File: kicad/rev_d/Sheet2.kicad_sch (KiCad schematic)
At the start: 226 parts, among them J10 vg_old, J5 external clock, J6 JUMPER, J8 JUMPER, J9 JUMPER, Q2 QUARTZ, Q3 QUARTZ32768, X10 ST-214C, X11 KEYB-MOUSE, X12 IDC20, X13 USB_C, X14 AAFP/AC97 audio, X15 PLB2-2, X16 PLB1-4I, X17 PLB1-4I, X18 PLB1-4I, X19 AVR pgm conn, X20 PLB1-4I, X21 RSA103, X4 IDC10M, X5 IDC10M, X6 RS232_9

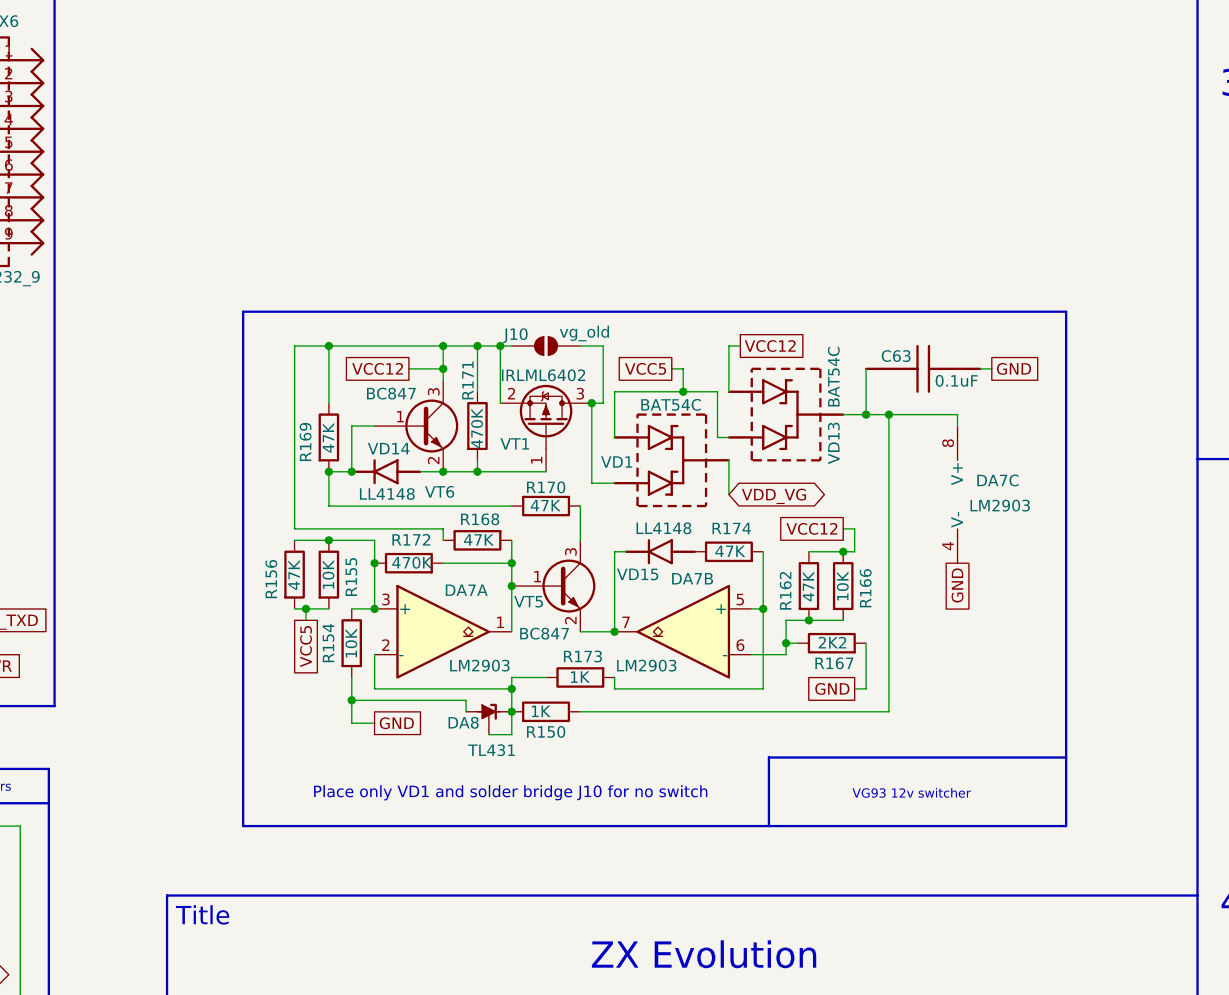
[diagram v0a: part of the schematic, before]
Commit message: pentevo: rev D: for VG 12v switcher, replace paralleled resistors with single ones
git-svn-id: svn://localhost/local-pentevo@1201 c6c76956-fad2-4150-a3a9-ea0a427205ba
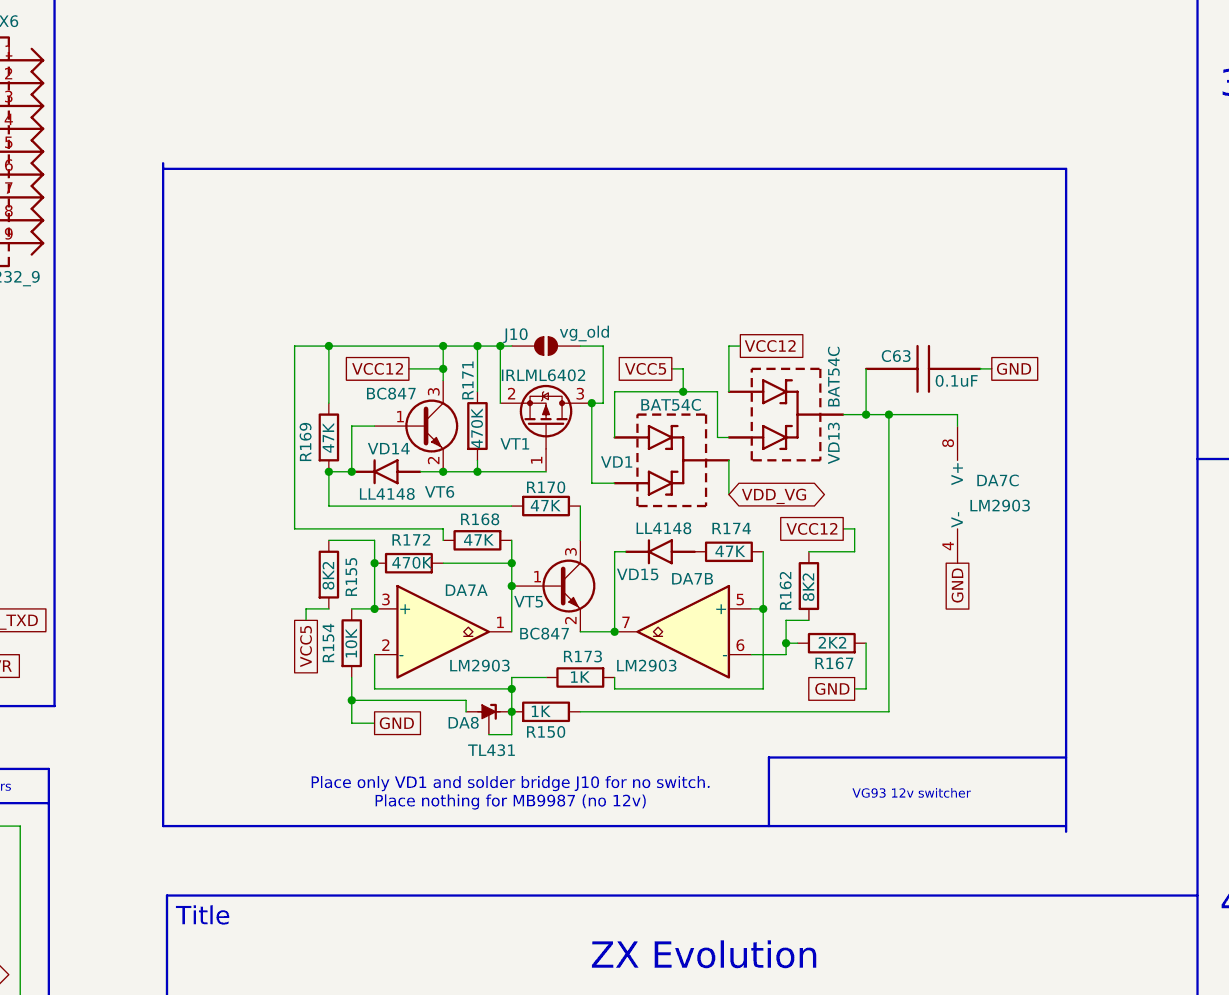
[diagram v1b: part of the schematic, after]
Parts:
- removed R156: 47K, Resistor_SMD:R_0805_2012Metric_Pad1.20x1.40mm_HandSolder, symbol Device:R
- removed R166: 10K, Resistor_SMD:R_0805_2012Metric_Pad1.20x1.40mm_HandSolder, symbol Device:R
- R155: value 10K -> 8K2
- R162: value 47K -> 8K2
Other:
- note added: "Place only VD1 and solder bridge J10 for no switch. Place nothing for MB9987 (no 12v)"
- note removed: "Place only VD1 and solder bridge J10 for no switch"
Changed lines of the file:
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@@
 	)
 	(junction
-		(at 499.11 335.28)
-		(diameter 0)
-		(color 0 0 0 0)
-	)
-	(junction
 		(at 161.29 233.68)
 		(diameter 0)
@@
 	)
 	(junction
-		(at 441.96 334.01)
-		(diameter 0)
-		(color 0 0 0 0)
-	)
-	(junction
 		(at 325.12 306.07)
 		(diameter 0)
@@
 	)
 	(junction
-		(at 439.42 341.63)
-		(diameter 0)
-		(color 0 0 0 0)
-	)
-	(junction
 		(at 492.76 345.44)
 		(diameter 0)
@@
 	)
 	(junction
-		(at 495.3 342.9)
-		(diameter 0)
-		(color 0 0 0 0)
-	)
-	(junction
 		(at 127 266.7)
 		(diameter 0)
@@
 	(wire
 		(pts
-			(xy 495.3 335.28) (xy 499.11 335.28)
+			(xy 495.3 335.28) (xy 500.38 335.28)
 		)
 		(stroke
@@
 	(wire
 		(pts
-			(xy 438.15 341.63) (xy 439.42 341.63)
-		)
-		(stroke
-			(width 0)
-			(type default)
-		)
-	)
-	(wire
-		(pts
 			(xy 383.54 288.29) (xy 384.81 288.29)
 		)
@@
 	(polyline
 		(pts
-			(xy 432.435 365.76) (xy 523.875 365.76)
+			(xy 423.545 365.76) (xy 523.875 365.76)
 		)
 		(stroke
@@
 	(wire
 		(pts
-			(xy 499.11 335.28) (xy 500.38 335.28)
-		)
-		(stroke
-			(width 0)
-			(type default)
-		)
-	)
-	(wire
-		(pts
 			(xy 391.16 213.36) (xy 386.08 213.36)
 		)
@@
 	(polyline
 		(pts
-			(xy 432.435 308.61) (xy 432.435 365.76)
+			(xy 423.545 292.1) (xy 423.545 365.76)
 		)
 		(stroke
@@
 	(wire
 		(pts
-			(xy 438.15 334.01) (xy 441.96 334.01)
-		)
-		(stroke
-			(width 0)
-			(type default)
-		)
-	)
-	(wire
-		(pts
 			(xy 346.71 74.93) (xy 346.71 105.41)
 		)
@@
 	(wire
 		(pts
-			(xy 495.3 342.9) (xy 499.11 342.9)
-		)
-		(stroke
-			(width 0)
-			(type default)
-		)
-	)
-	(wire
-		(pts
 			(xy 154.94 109.22) (xy 154.94 119.38)
 		)
@@
 	(polyline
 		(pts
-			(xy 523.875 365.76) (xy 523.875 308.61)
+			(xy 523.875 366.395) (xy 523.875 292.735)
 		)
 		(stroke
@@
 	(polyline
 		(pts
-			(xy 523.875 308.61) (xy 432.435 308.61)
+			(xy 523.875 292.735) (xy 423.545 292.735)
 		)
 		(stroke
@@
 		)
 	)
-	(text "Place only VD1 and solder bridge J10 for no switch"
+	(text "Place only VD1 and solder bridge J10 for no switch.\nPlace nothing for MB9987 (no 12v)"
 		(exclude_from_sim no)
 		(at 462.153 362.204 0)
@@
 			)
 		)
-		(property "Value" "10K"
+		(property "Value" "8K2"
 			(at 441.96 339.598 90)
 			(effects
@@
 	)
 	(symbol
-		(lib_id "Device:R")
-		(at 499.11 339.09 0)
-		(unit 1)
-		(exclude_from_sim no)
-		(in_bom yes)
-		(on_board yes)
-		(dnp no)
-		(property "Reference" "R166"
-			(at 501.65 341.63 90)
-			(effects
-				(font
-					(size 1.27 1.27)
-				)
-				(justify left)
-			)
-		)
-		(property "Value" "10K"
-			(at 499.11 340.868 90)
-			(effects
-				(font
-					(size 1.27 1.27)
-				)
-				(justify left)
-			)
-		)
-		(property "Footprint" "Resistor_SMD:R_0805_2012Metric_Pad1.20x1.40mm_HandSolder"
-			(at 497.332 339.09 90)
-			(effects
-				(font
-					(size 1.27 1.27)
-				)
-				(hide yes)
-			)
-		)
-		(property "Datasheet" "~"
-			(at 499.11 339.09 0)
-			(effects
-				(font
-					(size 1.27 1.27)
-				)
-				(hide yes)
-			)
-		)
-		(property "Description" "Resistor"
-			(at 499.11 339.09 0)
-			(effects
-				(font
-					(size 1.27 1.27)
-				)
-				(hide yes)
-			)
-		)
-		(pin "2"
-		)
-		(pin "1"
-		)
-		(instances
-			(project "eva"
-				(path "/ab605654-a730-497b-9e09-9b351f74b935/31d5864f-06ec-4c73-9256-780a6880087d"
-					(reference "R166")
-					(unit 1)
-				)
-			)
-		)
-	)
-	(symbol
 		(lib_id "Connector:Conn_01x01_Pin")
 		(at 292.1 213.36 0)
@@
 	)
 	(symbol
-		(lib_id "Device:R")
-		(at 438.15 337.82 0)
-		(unit 1)
-		(exclude_from_sim no)
-		(in_bom yes)
-		(on_board yes)
-		(dnp no)
-		(property "Reference" "R156"
-			(at 435.61 340.614 90)
-			(effects
-				(font
-					(size 1.27 1.27)
-				)
-				(justify left)
-			)
-		)
-		(property "Value" "47K"
-			(at 438.15 339.598 90)
-			(effects
-				(font
-					(size 1.27 1.27)
-				)
-				(justify left)
-			)
-		)
-		(property "Footprint" "Resistor_SMD:R_0805_2012Metric_Pad1.20x1.40mm_HandSolder"
-			(at 436.372 337.82 90)
-			(effects
-				(font
-					(size 1.27 1.27)
-				)
-				(hide yes)
-			)
-		)
-		(property "Datasheet" "~"
-			(at 438.15 337.82 0)
-			(effects
-				(font
-					(size 1.27 1.27)
-				)
-				(hide yes)
-			)
-		)
-		(property "Description" "Resistor"
-			(at 438.15 337.82 0)
-			(effects
-				(font
-					(size 1.27 1.27)
-				)
-				(hide yes)
-			)
-		)
-		(pin "2"
-		)
-		(pin "1"
-		)
-		(instances
-			(project "eva"
-				(path "/ab605654-a730-497b-9e09-9b351f74b935/31d5864f-06ec-4c73-9256-780a6880087d"
-					(reference "R156")
-					(unit 1)
-				)
-			)
-		)
-	)
-	(symbol
 		(lib_id "eva-altium-import:Sheet2_3_RESCHIP")
 		(at 100.33 314.96 0)
@@
 			)
 		)
-		(property "Value" "47K"
+		(property "Value" "8K2"
 			(at 495.3 340.868 90)
 			(effects

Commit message: pentevo: rev D: change VG 12v switcher schematics to have less components
git-svn-id: svn://localhost/local-pentevo@1202 c6c76956-fad2-4150-a3a9-ea0a427205ba
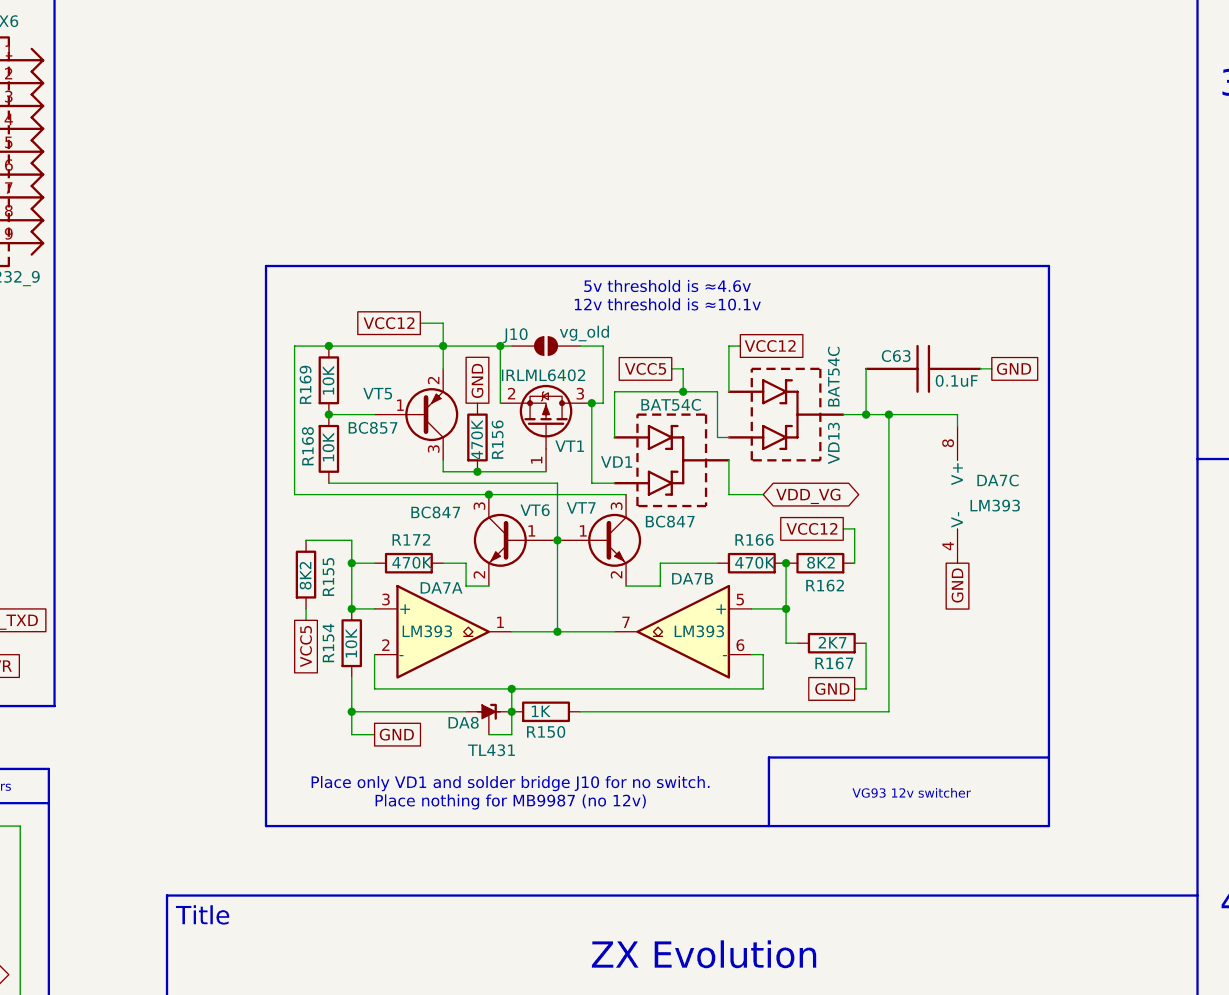
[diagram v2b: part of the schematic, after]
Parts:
- removed R170, R174: 47K, Resistor_SMD:R_0805_2012Metric_Pad1.20x1.40mm_HandSolder, symbol Device:R
- removed R171: 470K, Resistor_SMD:R_0805_2012Metric_Pad1.20x1.40mm_HandSolder, symbol Device:R
- removed R173: 1K, Resistor_SMD:R_0805_2012Metric_Pad1.20x1.40mm_HandSolder, symbol Device:R
- removed VD14, VD15: LL4148, Diode_SMD:D_MiniMELF_Handsoldering, symbol eva-altium-import:Sheet2_0_mirrored_LL4148
- removed VT5: BC847, Package_TO_SOT_SMD:SOT-23_Handsoldering, symbol Transistor_BJT:BC847
- added R156, R166: 470K, Resistor_SMD:R_0805_2012Metric_Pad1.20x1.40mm_HandSolder, symbol Device:R
- added VT5: BC857, Package_TO_SOT_SMD:SOT-23_Handsoldering, symbol Transistor_BJT:BC857
- added VT7: BC847, Package_TO_SOT_SMD:SOT-23, symbol Transistor_BJT:BC847
- DA7: value LM2903 -> LM393
- R167: value 2K2 -> 2K7
- R168, R169: value 47K -> 10K
- VT6: footprint Package_TO_SOT_SMD:SOT-23_Handsoldering -> Package_TO_SOT_SMD:SOT-23
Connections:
- net GND: now also R156.1
- net VCC12: now also R162.2, VT5.2 (E), VT7.3 (C); no longer R162.1, R168.1
- net at DA7.7: now also DA7.1, R168.1, VT6.1 (B), VT7.1 (B)
- net at DA7.5 (+): now also R162.1, R167.1, R166.2
- net at VT6.2 (E): now also R172.2; no longer VT1.1 (G)
- net at R169.2: now also R168.2, VT5.1 (B); no longer VT6.1 (B)
- net at DA7.2 (-), DA8.1 (K), DA8.2 (REF)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: now also DA7.6 (-)
- new net: R166.1, VT7.2 (E)
- new net: R156.2, VT1.1 (G), VT5.3 (C)
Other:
- note added: "5v threshold is ≈4.6v 12v threshold is ≈10.1v"
- moved on the sheet: R155, R162, R169

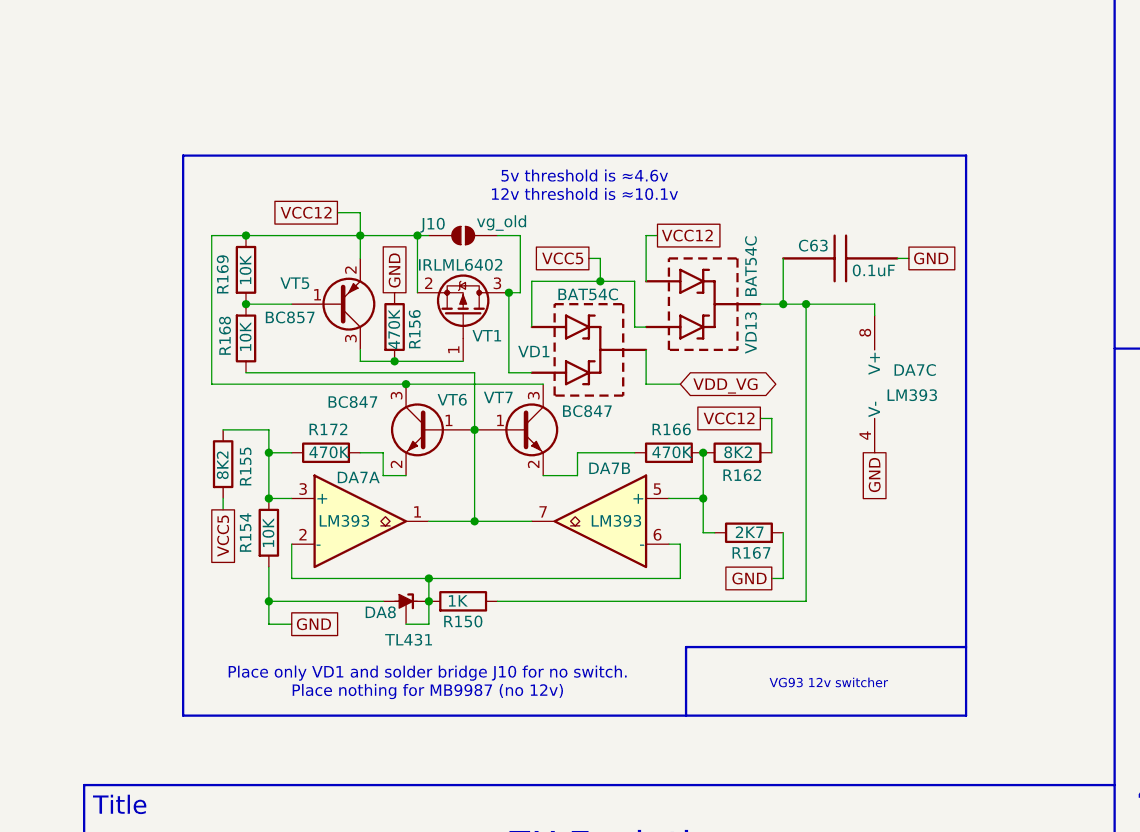
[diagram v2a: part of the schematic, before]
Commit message: pentevo: rev D: change VG 12v switcher schematics to using 2xPST529C, results in significantly less components
git-svn-id: svn://localhost/local-pentevo@1205 c6c76956-fad2-4150-a3a9-ea0a427205ba
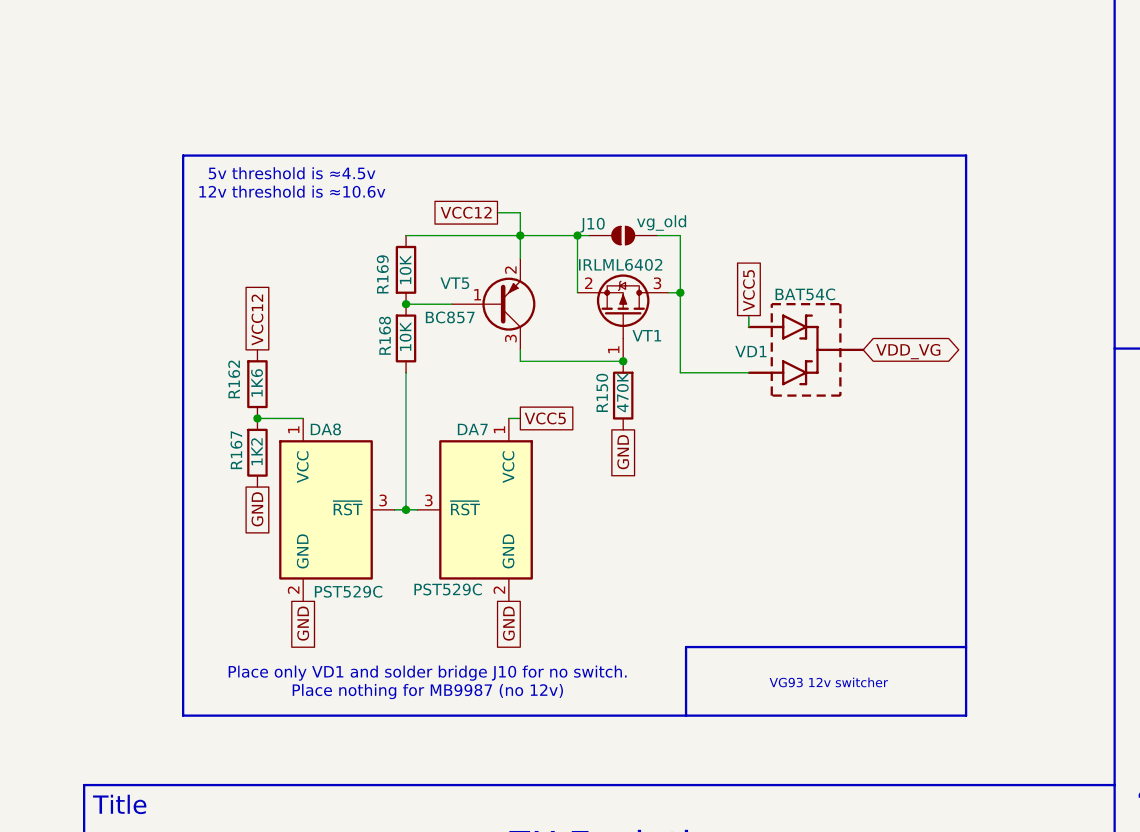
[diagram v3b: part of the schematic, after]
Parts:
- removed C63: 0.1uF, Capacitor_SMD:C_0805_2012Metric_Pad1.18x1.45mm_HandSolder, symbol eva-altium-import:Sheet1_0_CAPCHIP
- removed DA7: LM393, Package_SO:SOIC-8_3.9x4.9mm_P1.27mm, symbol Comparator:LM2903
- removed DA8: TL431, Package_TO_SOT_SMD:SOT-23_Handsoldering, symbol Reference_Voltage:TL431DBZ
- removed R154: 10K, Resistor_SMD:R_0805_2012Metric_Pad1.20x1.40mm_HandSolder, symbol Device:R
- removed R155: 8K2, Resistor_SMD:R_0805_2012Metric_Pad1.20x1.40mm_HandSolder, symbol Device:R
- removed R156, R166, R172: 470K, Resistor_SMD:R_0805_2012Metric_Pad1.20x1.40mm_HandSolder, symbol Device:R
- removed VD13: BAT54C, Package_TO_SOT_SMD:SOT-23_Handsoldering, symbol eva-altium-import:Sheet1_2_BAT54C
- removed VT6, VT7: BC847, Package_TO_SOT_SMD:SOT-23, symbol Transistor_BJT:BC847
- added DA7, DA8: PST529C, Package_TO_SOT_THT:TO-92_HandSolder, symbol eva-altium-import:PST529C
- R150: value 1K -> 470K
- R162: value 8K2 -> 1K6
- R167: value 2K7 -> 1K2
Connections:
- net GND: now also R150.1, R167.1, DA7.2 (GND), DA8.2 (GND); no longer R167.2
- net VCC5: now also DA7.1 (VCC)
- net at R162.1: now also R167.2, DA8.1 (VCC); no longer R167.1
- net at R168.1: now also DA7.3 (~{RST}), DA8.3 (~{RST})
- net at R150.2: now also VT1.1 (G), VT5.3 (C)
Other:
- note added: "5v threshold is ≈4.5v 12v threshold is ≈10.6v"
- note removed: "5v threshold is ≈4.6v 12v threshold is ≈10.1v"
- moved on the sheet: J10, R162, R167, R168, R169, VD1, VT1, VT5
